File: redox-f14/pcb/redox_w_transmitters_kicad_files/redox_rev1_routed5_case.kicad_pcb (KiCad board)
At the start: 2 copper layers, 145.8 x 126.5 mm, 31 parts, among them K0 KEYSW, K1 KEYSW, K10 KEYSW, K11 KEYSW, K12 KEYSW, K13 KEYSW, K14 KEYSW, K15 KEYSW, K16 KEYSW, K2 KEYSW, K20 KEYSW, K21 KEYSW, K22 KEYSW, K23 KEYSW, K24 KEYSW, K25 KEYSW, K26 KEYSW, K3 KEYSW, K30 KEYSW, K31 KEYSW, K32 KEYSW, K33 KEYSW, K34 KEYSW, K35 KEYSW, K4 KEYSW, K42 KEYSW, K43 KEYSW, K44 KEYSW, K45 KEYSW, K5 KEYSW, K6 KEYSW

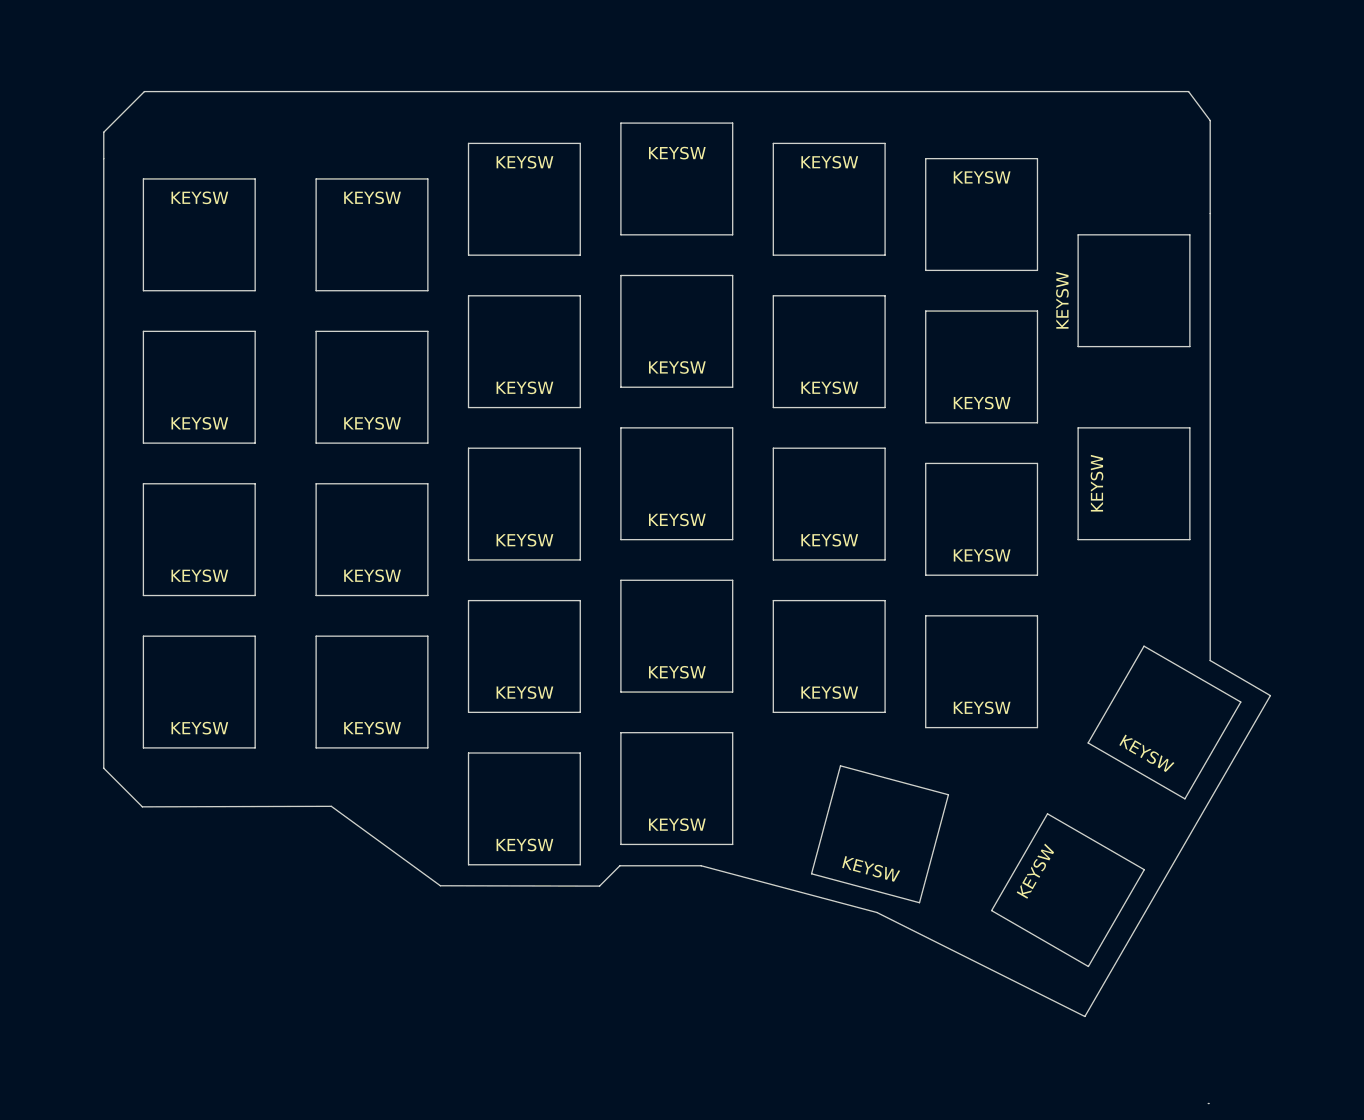
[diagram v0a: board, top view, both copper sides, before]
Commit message: add case files
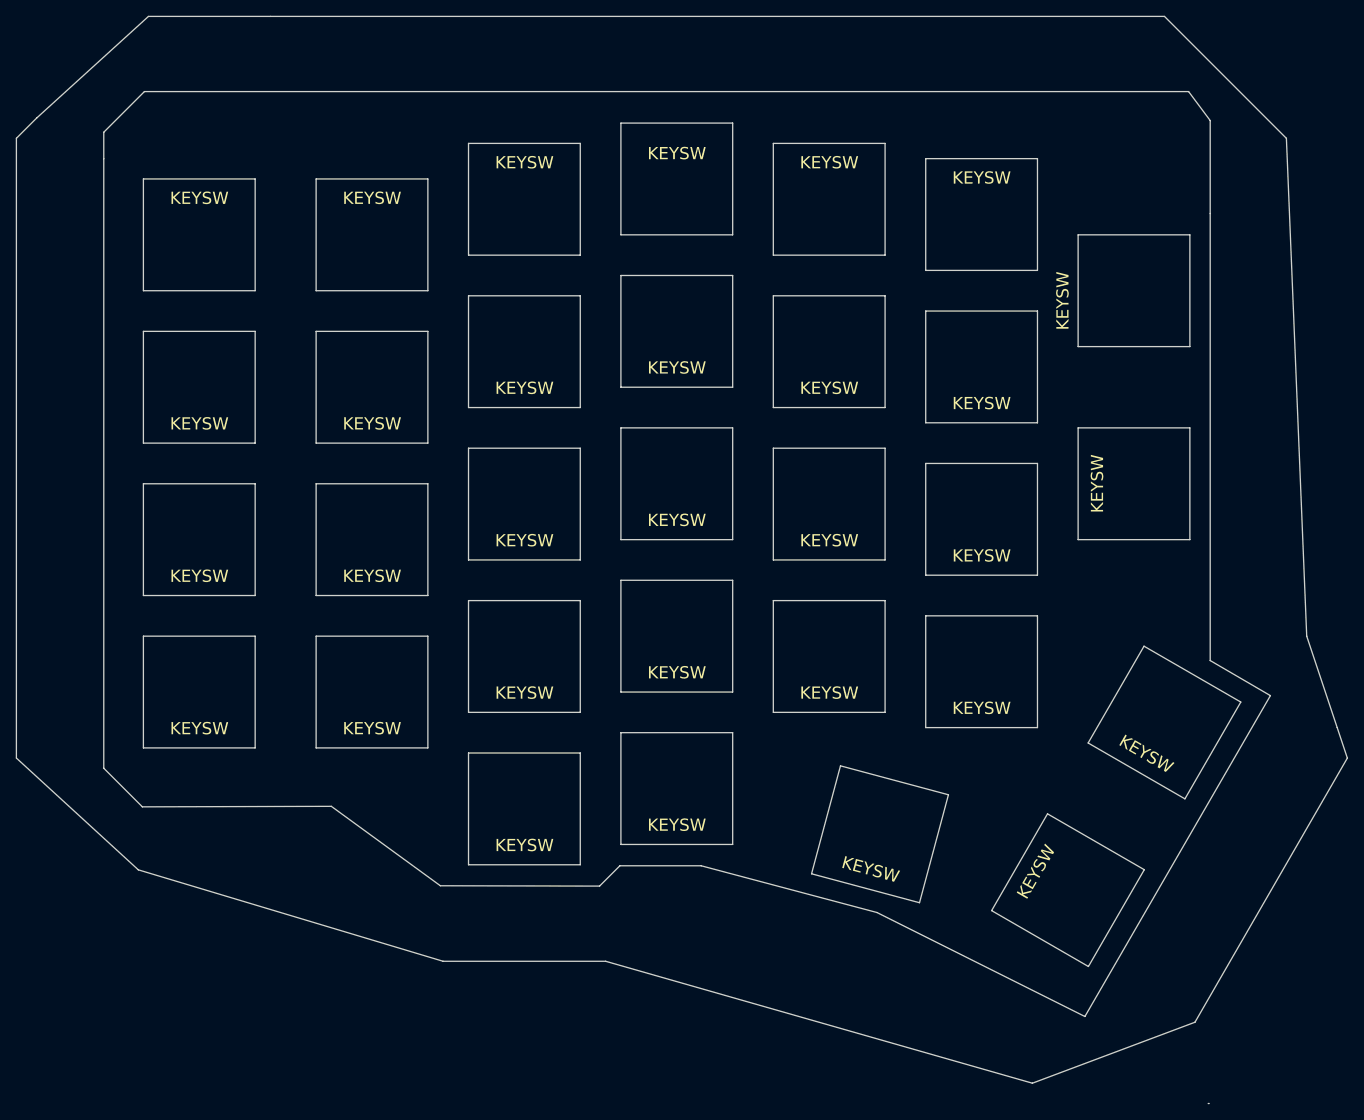
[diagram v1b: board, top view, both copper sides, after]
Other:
- board size 145.8 x 126.5 mm -> 166.4 x 135.9 mm
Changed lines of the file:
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@@
   (general
     (thickness 1.6)
-    (drawings 18)
+    (drawings 33)
     (tracks 0)
     (zones 0)
@@
     )
   )
+  (gr_line (start 68.58 54.61) (end 68.58 132.08) (layer Edge.Cuts) (width 0.1))
+  (gr_line (start 71.12 52.07) (end 68.58 54.61) (layer Edge.Cuts) (width 0.1))
+  (gr_line (start 71.12 52.07) (end 85.09 39.37) (layer Edge.Cuts) (width 0.1))
+  (gr_line (start 83.82 146.05) (end 68.58 132.08) (layer Edge.Cuts) (width 0.1))
+  (gr_line (start 121.92 157.48) (end 83.82 146.05) (layer Edge.Cuts) (width 0.1))
+  (gr_line (start 142.24 157.48) (end 121.92 157.48) (layer Edge.Cuts) (width 0.1))
+  (gr_line (start 195.58 172.72) (end 142.24 157.48) (layer Edge.Cuts) (width 0.1))
+  (gr_line (start 215.9 165.1) (end 195.58 172.72) (layer Edge.Cuts) (width 0.1))
+  (gr_line (start 234.95 132.08) (end 215.9 165.1) (layer Edge.Cuts) (width 0.1))
+  (gr_line (start 233.68 128.27) (end 234.95 132.08) (layer Edge.Cuts) (width 0.1))
+  (gr_line (start 229.87 116.84) (end 233.68 128.27) (layer Edge.Cuts) (width 0.1))
+  (gr_line (start 227.33 54.61) (end 229.87 116.84) (layer Edge.Cuts) (width 0.1))
+  (gr_line (start 212.09 39.37) (end 227.33 54.61) (layer Edge.Cuts) (width 0.1))
+  (gr_line (start 100.33 39.37) (end 212.09 39.37) (layer Edge.Cuts) (width 0.1))
+  (gr_line (start 85.09 39.37) (end 100.33 39.37) (layer Edge.Cuts) (width 0.1))
   (gr_line (start 215.10625 48.768) (end 217.805 52.3875) (layer Edge.Cuts) (width 0.1))
   (gr_line (start 107.95 138.1125) (end 84.328 138.176) (layer Edge.Cuts) (width 0.1))
